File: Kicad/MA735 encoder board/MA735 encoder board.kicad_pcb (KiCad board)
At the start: 2 copper layers, 5.7 x 80.4 mm, 4 parts, among them J1 FPC contacts 0.3mm, U1 MA735GGU-Z

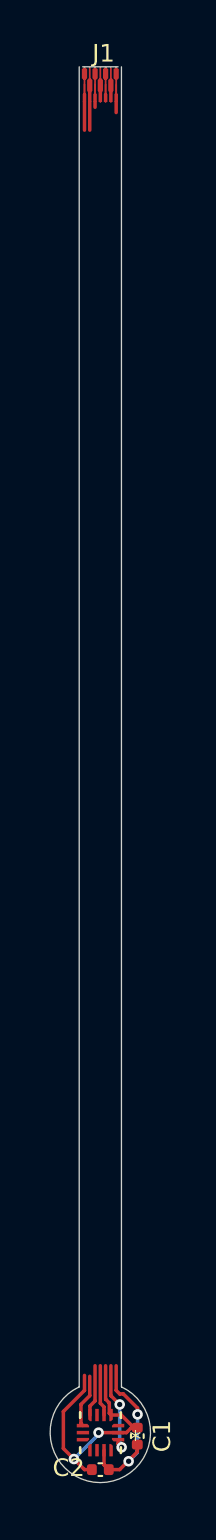
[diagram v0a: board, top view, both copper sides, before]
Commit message: Finished Magnetic encoder flex pcb
I added a hatched ground plane. I also re-arranged the filter capacitors so the clock signal could get out without needing vias. There is much more room now with the wiring
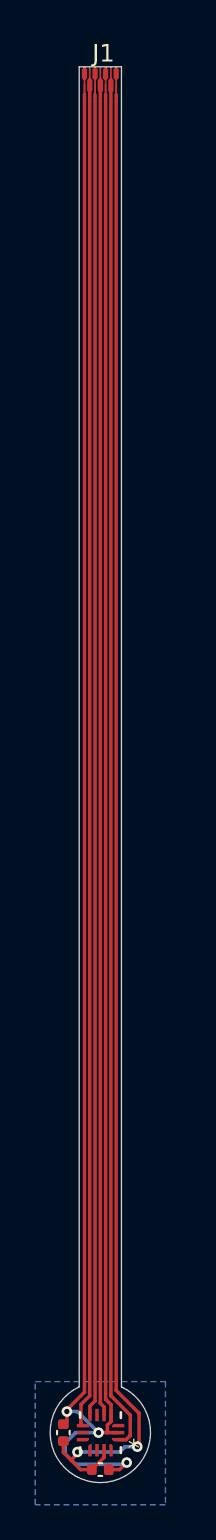
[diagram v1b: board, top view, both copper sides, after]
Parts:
- moved C1 4.20 mm to (150.7, 131.7)
- turned C2 to 0 degrees
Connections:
- J1 pad 1: /MOSI -> GND
- J1 pad 2: GND -> /MOSI
- J1 pad 3: /MISO -> /CS
- J1 pad 4: GND -> /MISO
- J1 pad 5: /SCK -> GND
- J1 pad 6: +3V3 -> /SCK
- J1 pad 7: /CS -> +3V3
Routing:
- net GND: track 19.5 -> 164.8 mm, vias 2 -> 3
- net +3V3: track 10.9 -> 86.2 mm
- net /SCK: track 6.41 -> 78.0 mm, vias 2 -> 0
- net /MISO: track 4.19 -> 75.7 mm
- net /CS: track 4.52 -> 75.7 mm
- net /MOSI: track 5.65 -> 76.5 mm
- added copper zone on B.Cu, net GND
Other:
- outline, holes or cut-outs redrawn
- board text removed: "Minimum solder mask is 0.5mm. I have to remove more around the edge connector and the encode"
